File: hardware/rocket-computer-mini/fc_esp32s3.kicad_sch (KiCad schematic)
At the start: 31 parts, among them SW2 R-667995, U32 ESP32-S3RH2, U33 GD25Q128ESIG, Y3 ABS07-32.768KHZ-T, Y4 ECS-400-10-37B2-CKY-TR

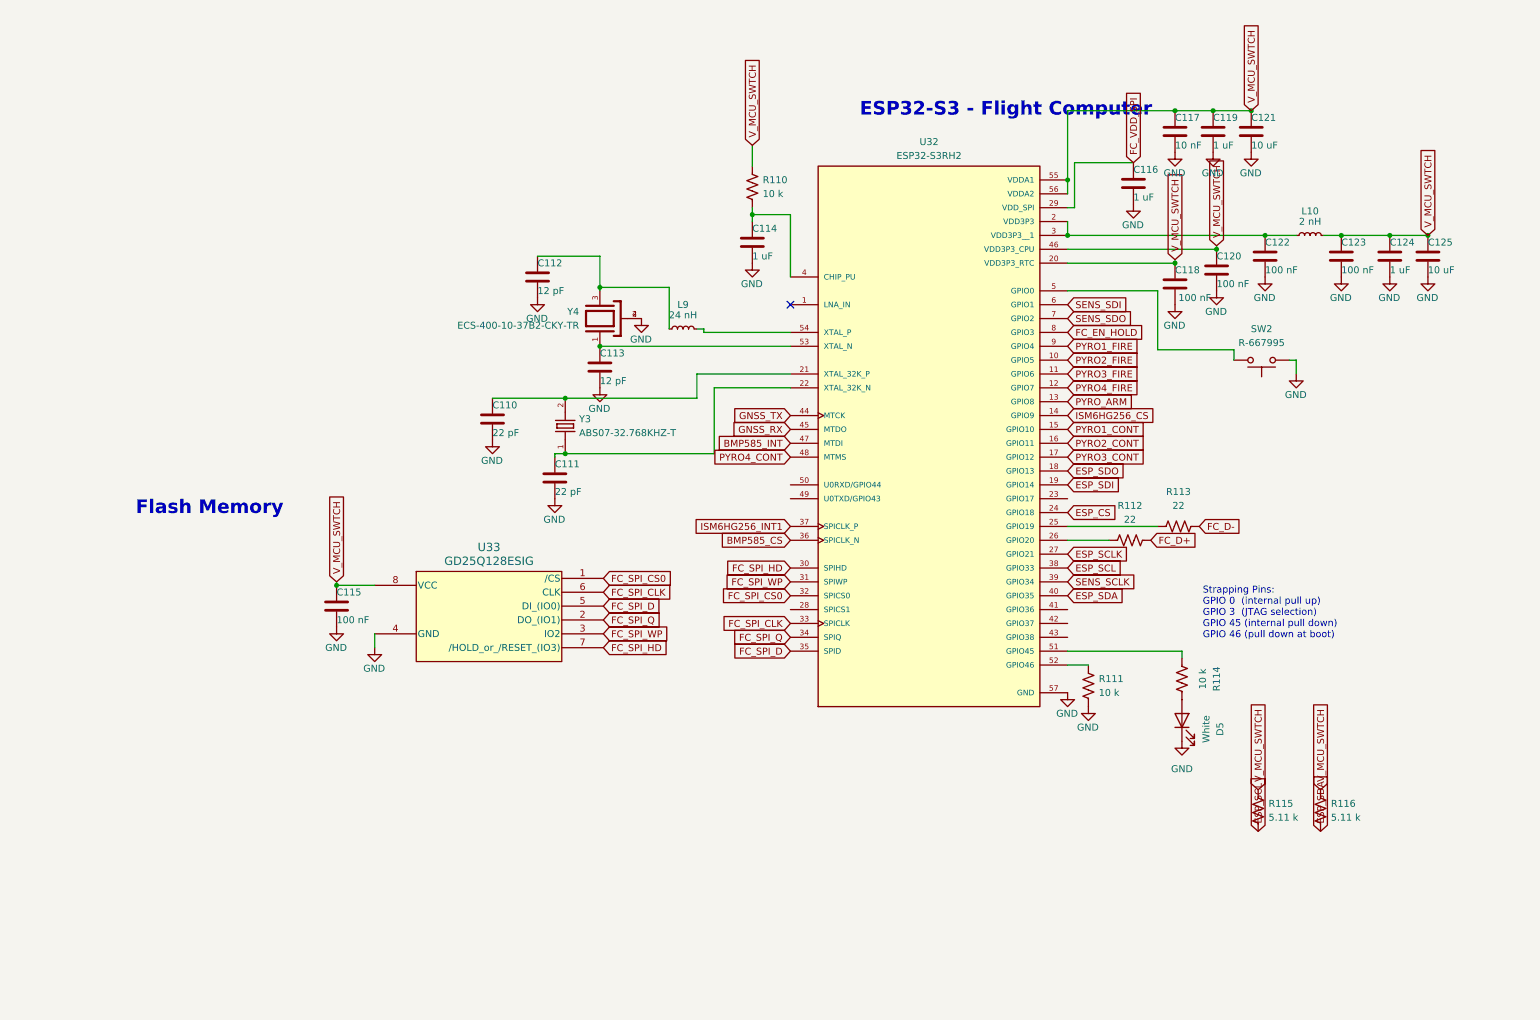
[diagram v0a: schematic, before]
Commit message: hardware(rocket-computer-mini): get both processors off a floating GPIO3
pin-budget.md justified GPIO3 in one sentence -- "GPIO3 is safe here, it
drives a switch enable and its pulldown holds it low at reset". Adding the
second processor invalidated that on BOTH parts, and neither failure was
visible in ERC or the netlist:

  - Flight computer: GPIO3 was still the switch enable, but D9 now stands
    between the pin and R84, and a diode does not pass a pulldown. The very
    change that created the enable OR is what removed the pull.
  - Out computer: GPIO3 stopped being the enable (that moved to GPIO7) and
    became ESP_SDO -- an INPUT driven by the flight computer, which is
    unpowered while the out computer boots, so the net floated.

FC_EN_HOLD moves from GPIO3 to GPIO17, leaving the flight computer's
strapping pin a bare pad with no trace on it. R34 (100 k) pulls ESP_SDO
down so the out computer's GPIO3 has a defined level at reset.

GPIO17 is not an arbitrary choice. rocket-computer closed #825/#848 in
firmware (PR #859) by driving the hold pin HIGH *and* calling gpio_hold_en,
so the pad stays latched through the FC's own panic/WDT resets -- without
that, an FC crash mid-flight drops the rail and takes all four pyro
channels with it. On the ESP32-S3 gpio_hold_en only reaches the
reset-surviving RTC latch for RTC-capable pads: esp_driver_gpio/gpio.c
dispatches to rtc_gpio_hold_en when rtc_gpio_is_valid_gpio passes and
otherwise falls back to the deep-sleep-only digital hold. This part has
SOC_RTCIO_PIN_COUNT = 22 (GPIO0-GPIO21) and RTCIO_GPIO17_CHANNEL exists,
so GPIO17 latches exactly the way the P4's GPIO5 does. Both docs now carry
that as a hard constraint on the board header, because moving the pin above
GPIO21 still returns ESP_OK and fails silently.

Keeping the hold on GPIO3 would also have coupled the power latch to boot
configuration: gpio_hold_en would have held a strapping pin HIGH through
every in-flight reset.

Doc corrections that came out of t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
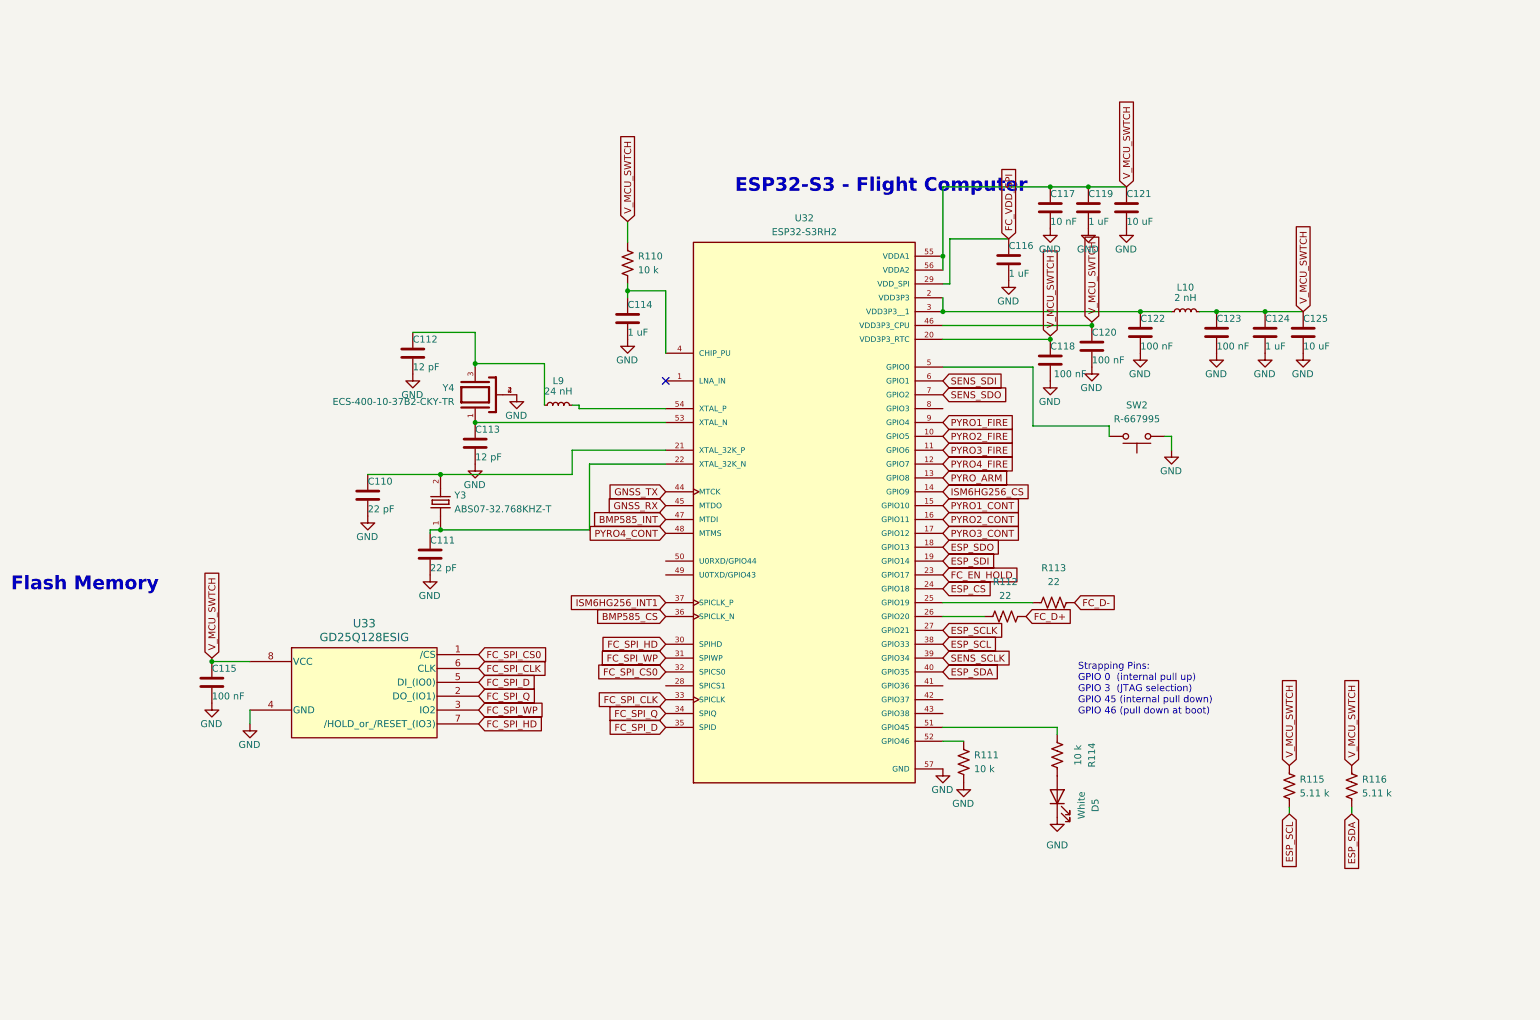
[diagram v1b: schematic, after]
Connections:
- net FC_EN_HOLD: now also U32.23 (GPIO17); no longer U32.8 (GPIO3)
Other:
- moved on the sheet: C110, C111, C112, C113, C114, C115, C116, C117, C118, C119, C120, C121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

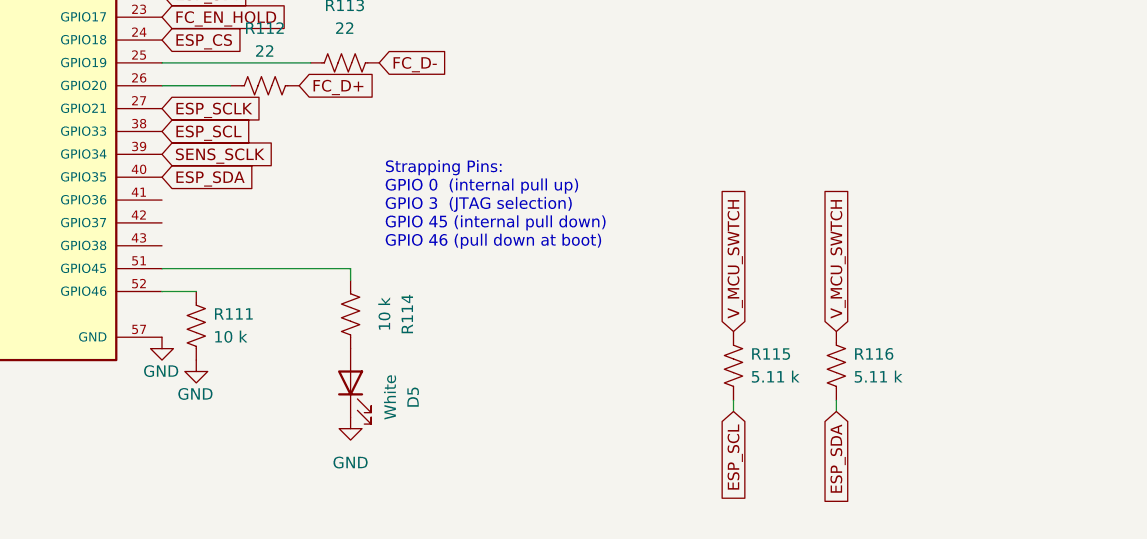
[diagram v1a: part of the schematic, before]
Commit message: mini: the magnetometer belongs to the flight computer
It is a flight sensor and it was on the wrong processor. The IMU, the
barometer and the GNSS all sit on the flight computer; the magnetometer
alone hung off the out computer's power-monitor I2C bus. That was a
single-MCU decision -- pin-budget.md's "shares the power-monitor I2C bus,
no new pins" -- and nothing revisited it when the board grew a second
processor. rocket-computer has always put its IIS2MDCTR on the flight
computer's own bus with the pull-ups on the same rail as the part.

Being stranded there broke it in two independent ways:

  * Electrically. R67/R69 pull up to +3V3 while U3's supply sat behind U30,
    whose QOD ACTIVELY discharges the rail. In pad standby those pull-ups
    drove its I2C pads against a grounded supply -- above abs-max, clamping
    the bus below VIL, and making the INA230 unreadable. That is the whole
    of the board's battery telemetry; nothing else reaches VBAT.
  * In firmware. Every magnetometer driver in the tree is built into
    flight_computer, which cannot reach a part on the other processor's
    bus, so the board had no heading source at all.

The previous commit addressed only the first, by moving U3's supply to
+3V3. That treated the symptom -- correct as far as it went, but it left a
flight sensor on the comms processor. This moves the part instead:

  U3 SCL/SDA  -> MAG_SCL / MAG_SDA on the FC, GPIO37 / GPIO36
  R117/R118   -> 5.11 k pull-ups on V_MCU_SWTCH, the part's own rail
  U3 VDD      -> back to V_MCU_SWTCH with the other three sensors
  SEN_SCL/SDA -> pure pack-monitor bus on +3V3 (U15 + U23 + R67/R69),
                 the same shape as rocket-computer's PWR_SCL/PWR_SDA

Now the part, its master and its pull-ups all share one rail, so no passive
pull-up crosses the rail boundary at all -- every remaining crossing is an
actively driven signal firmware can park Hi-Z.

Firmware follows: flight_computer/board_m1.h gets IIS2MDC_SDA=36,
IIS2MDC_SCL=37 and USE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
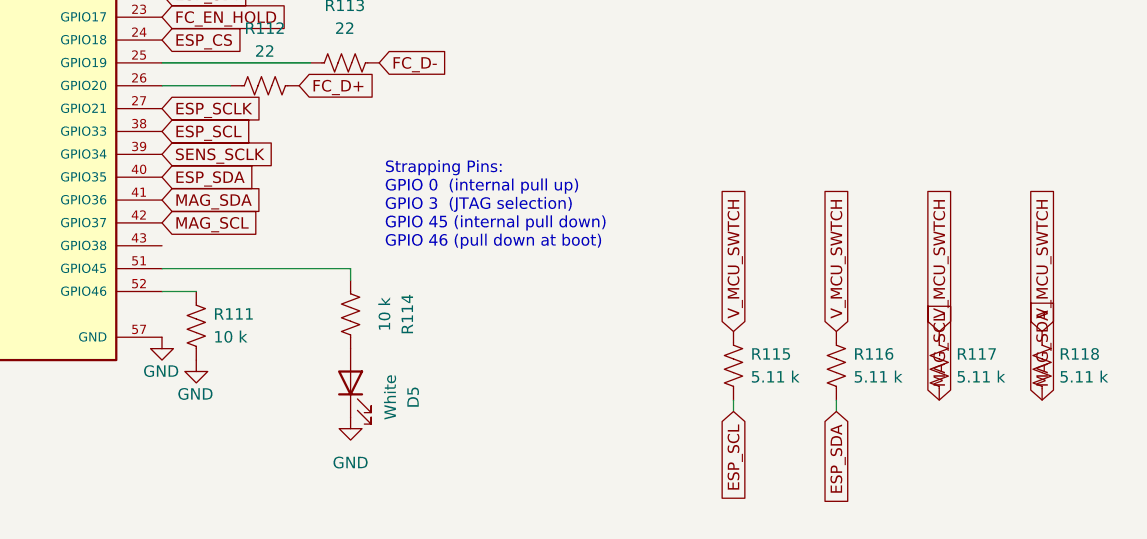
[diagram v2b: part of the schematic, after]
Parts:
- added R117, R118: 5.11 k, Resistor_SMD:R_0402_1005Metric, symbol Device:R_US
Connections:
- net V_MCU_SWTCH: now also R117.1, R118.1
- net MAG_SDA: now reaches U32.41 (GPIO36)
- net MAG_SDA: now also R118.2
- net MAG_SCL: now reaches U32.42 (GPIO37)
- net MAG_SCL: now also R117.2

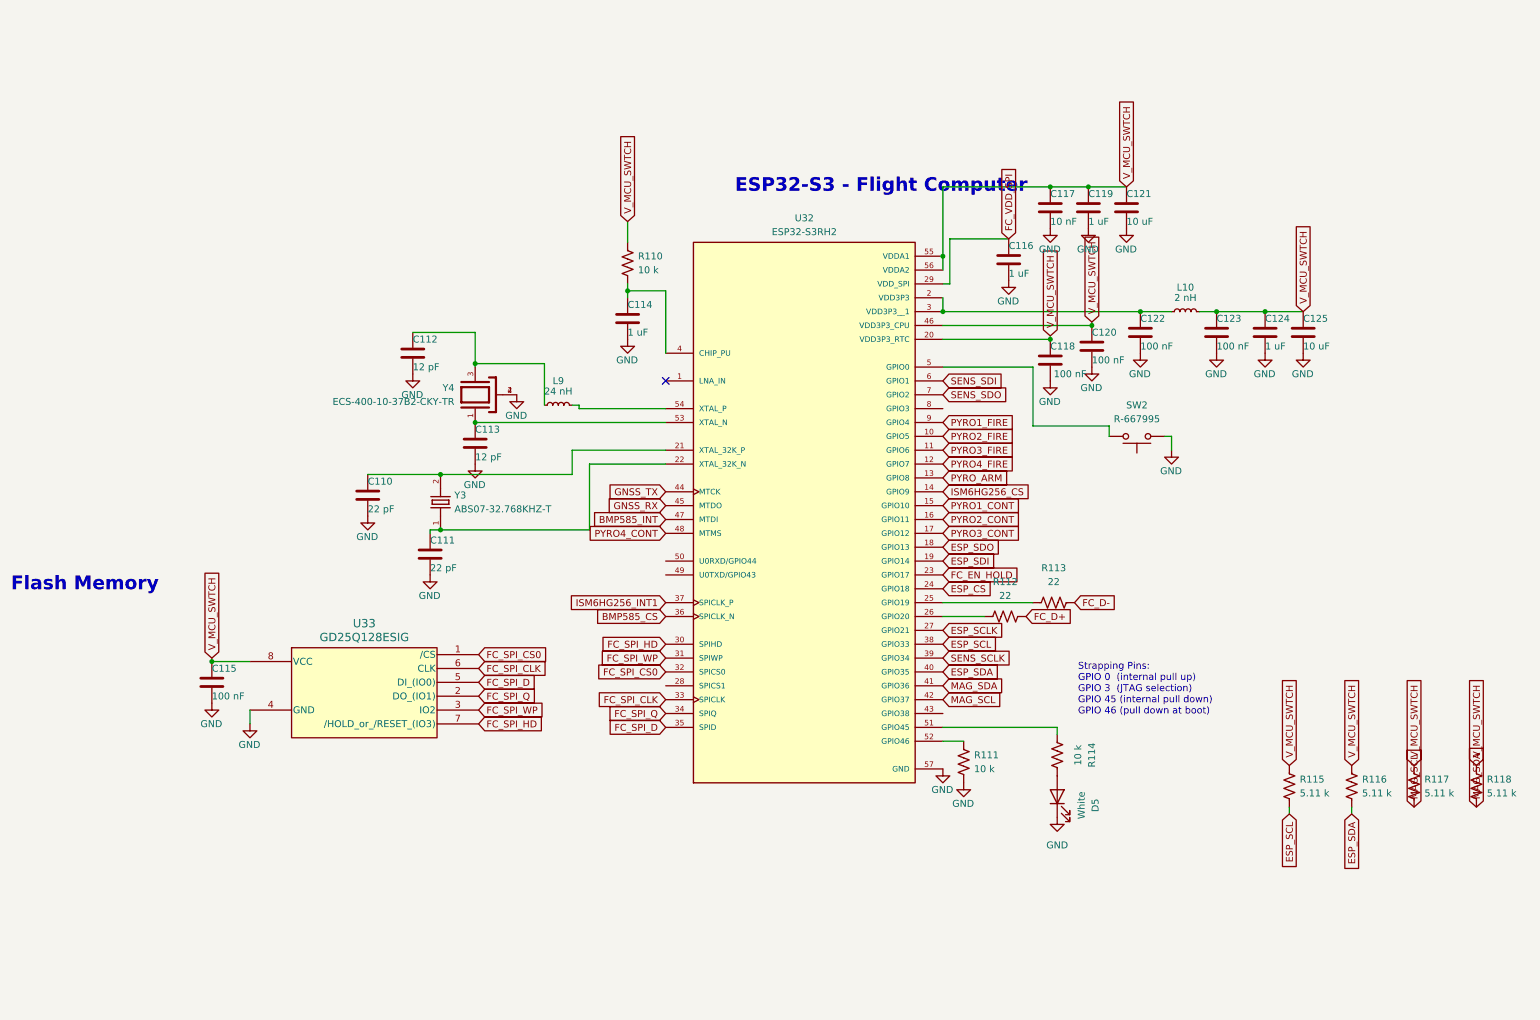
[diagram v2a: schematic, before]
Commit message: hardware: pack-direct pyro + supercap hold-up on both rocket computers (WIP)
rocket-computer-mini:
- pyro store deleted; channels fire from VBAT_CON (pack-direct, upstream
  of the 0.9 A eFuse). PYRO_FIRE_DURATION is a live knob again.
- ARM is a charge-pump dead-man (ARM_CLK on FC GPIO8, ex-PYRO_ARM; a
  static GPIO can never arm) with a latching hardware ceiling that times
  ARM_GATE itself (1.5-3.3 s; release = FC-domain power cycle).
- +3V3 hold-up: V_BUCK -> LM66100 -> V_HOLD -> TPS22810 -> +3V3 with a
  2 F supercap (CHP5R5L205R-TWQ) behind 33R charge / LM66100 discharge,
  TPS3840PL29 cutting cleanly at 2.86-2.94 V. Both LM66100 CE pins tie
  to VOUT (reverse blocking); U40 ST is CAP_ACTIVE (low=buck, high=cap).
- DEF tied to V_BUCK (3.465 V rail); CAP_ACTIVE to both MCUs;
  V_SCAP_ADC on OC GPIO8. Console UART fully restored.
- PCB re-synced to the schematic; 76 dangling P4-era segments/vias and
  6 dead zones purged, all fills regenerated (97 stale-fill clearance
  violations cleared); schematic parity: 0 violations. No outline yet.

rocket-computer (V10): same architecture drawn as off-page blocks with
the same refdes; 2x supercaps for the 0.5-0.8 A dual-MCU load; V_CAP ->
VBAT_CON; C94 1u -> 4.7u so a 500 ms firing sag cannot open the eFuse
(GNSS daughterboards ride the raw sag; TPS62913 input floor ~3.8 V).
P4 pad 17 = ARM_CLK, pad 18 = V_SCAP_ADC, PIEZZO moved to the S3.
MANUAL: the V_BUCK rail split at U18 (note on the power sheet).

docs: firmware-notes.md (BOD to 2.44 V both MCUs, CAP_ACTIVE handler,
shed order, ARM spacing) and pack-fire-holdup-options.md (options A-D,
complications register). New prismatic supercap footprint; shared
footprint refreshes from the KiCad sessions.

Both boards are WIP: mini layout not started, V10 splice pending.

Co-Authored-By: Claude Fable 5 <noreply@anthropic.com>
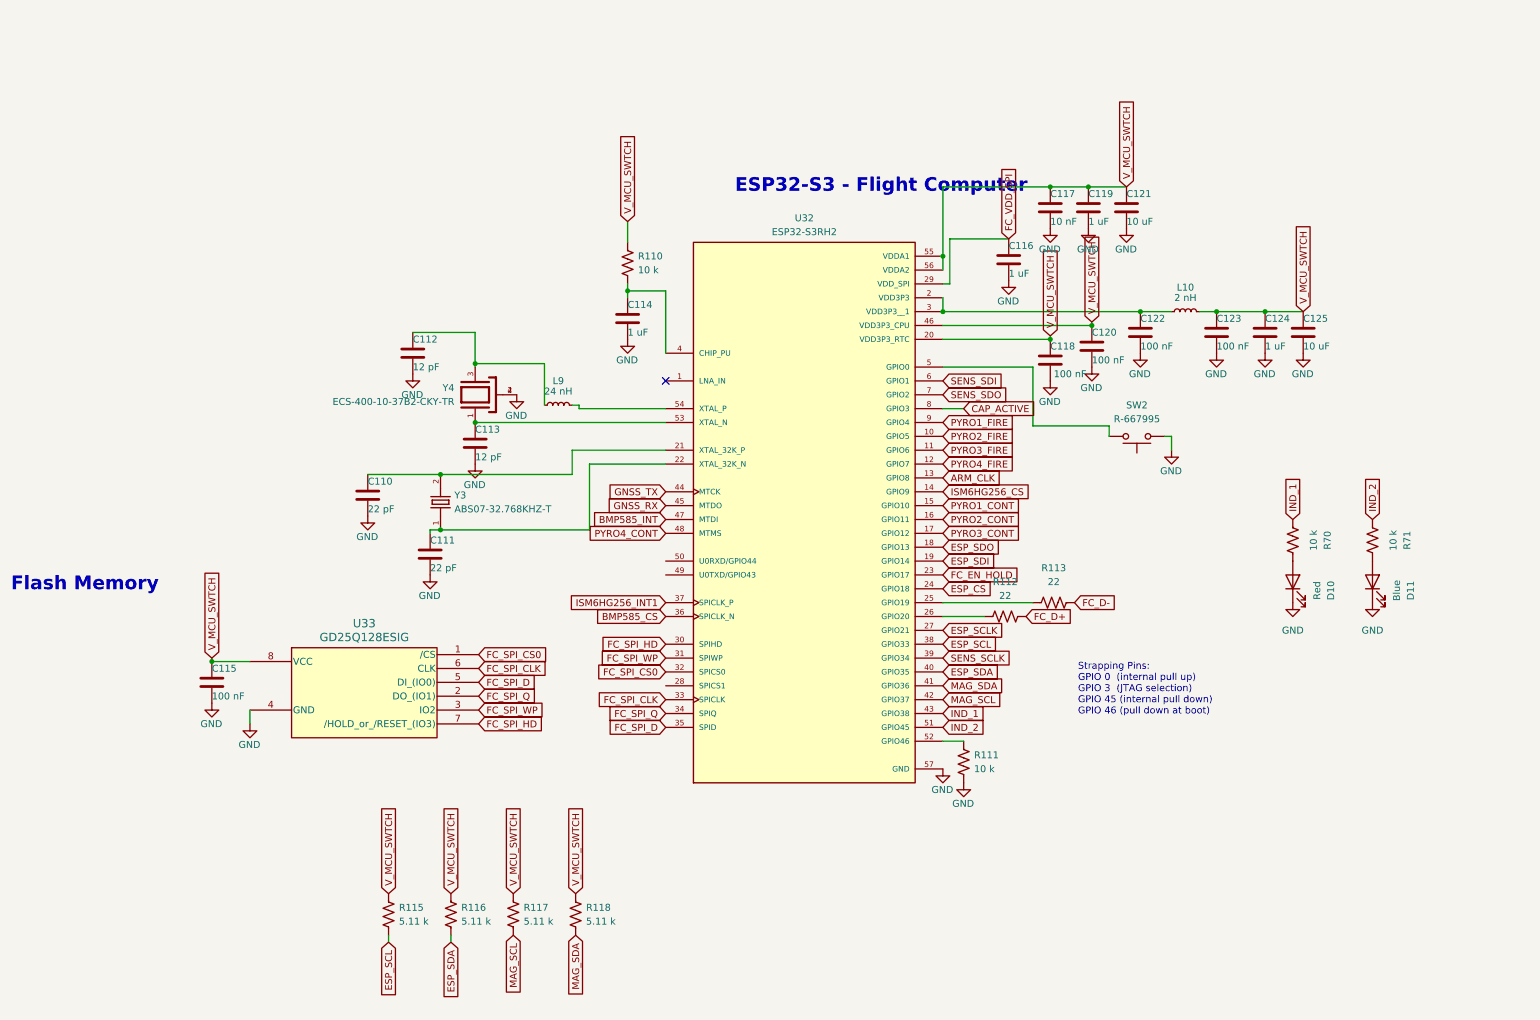
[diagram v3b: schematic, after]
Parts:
- removed D5: White, LED_SMD:LED_0402_1005Metric, symbol Device:LED
- removed R114: 10 k, Resistor_SMD:R_0402_1005Metric, symbol Device:R_US
- added D10: Red, LED_SMD:LED_0402_1005Metric, symbol Device:LED
- added D11: Blue, LED_SMD:LED_0402_1005Metric, symbol Device:LED
- added R70, R71: 10 k, Resistor_SMD:R_0402_1005Metric, symbol Device:R_US
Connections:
- net GND: now also D10.1 (K), D11.1 (K)
- net IND_1: now reaches U32.43 (GPIO38)
- net IND_1: now also R70.1
- net IND_2: now reaches U32.51 (GPIO45)
- net IND_2: now also R71.1
- net CAP_ACTIVE: now reaches U32.8 (GPIO3)
- net PYRO_ARM renamed ARM_CLK
- new net: D10.2 (A), R70.2
- new net: D11.2 (A), R71.2
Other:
- moved on the sheet: R115, R116, R117, R118
